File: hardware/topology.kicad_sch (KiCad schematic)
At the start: 0 parts

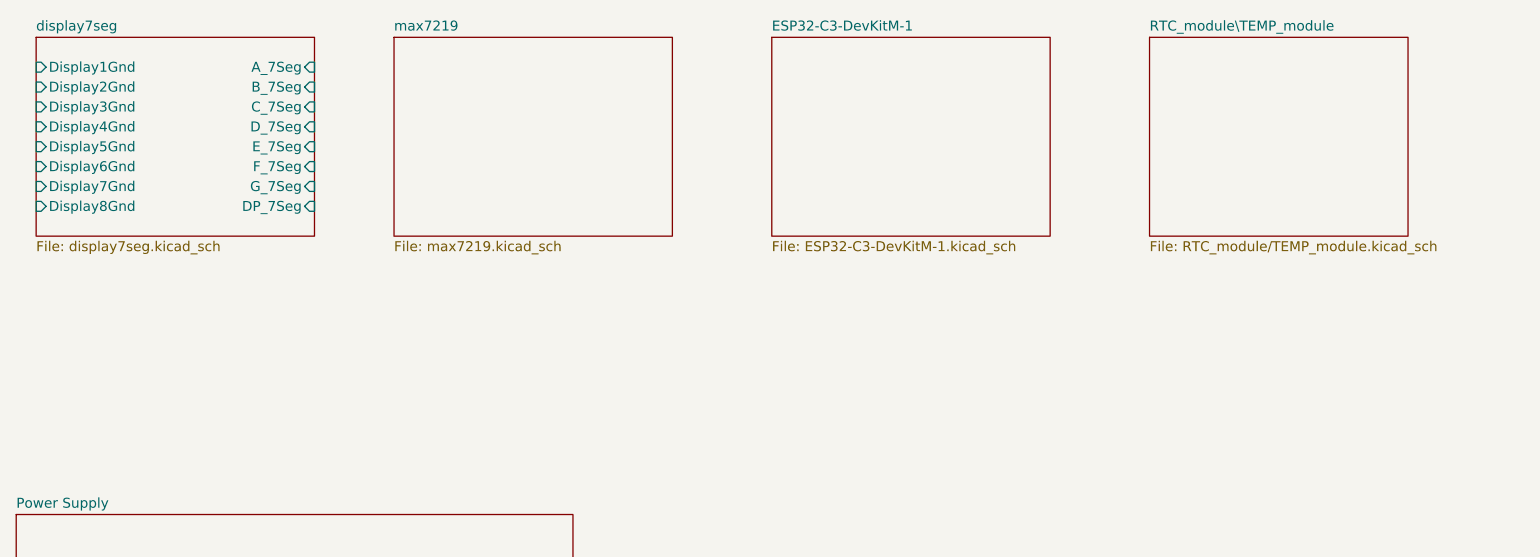
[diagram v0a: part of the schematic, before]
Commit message: Hardware: Rename Temp to RTC-Sensor and Update Schematics
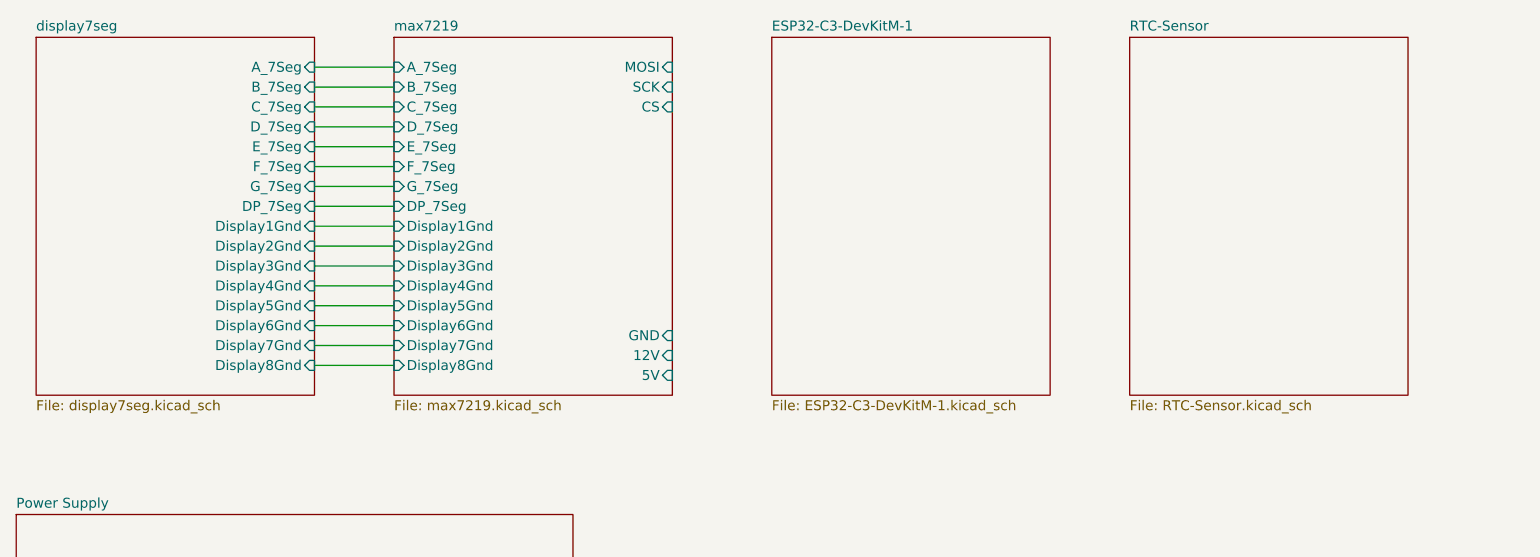
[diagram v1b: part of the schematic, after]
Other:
- removed sheet RTC_module\TEMP_module
- added sheet RTC-Sensor (RTC-Sensor.kicad_sch)
- sheet max7219 ports: added 12V, 5V, A_7Seg, B_7Seg, CS, C_7Seg, DP_7Seg, D_7Seg, Display1Gnd, Display2Gnd, Display3Gnd, Display4Gnd, Display5Gnd, Display6Gnd, Display7Gnd, Display8Gnd, E_7Seg, F_7Seg, GND, G_7Seg, MOSI, SCK; removed none

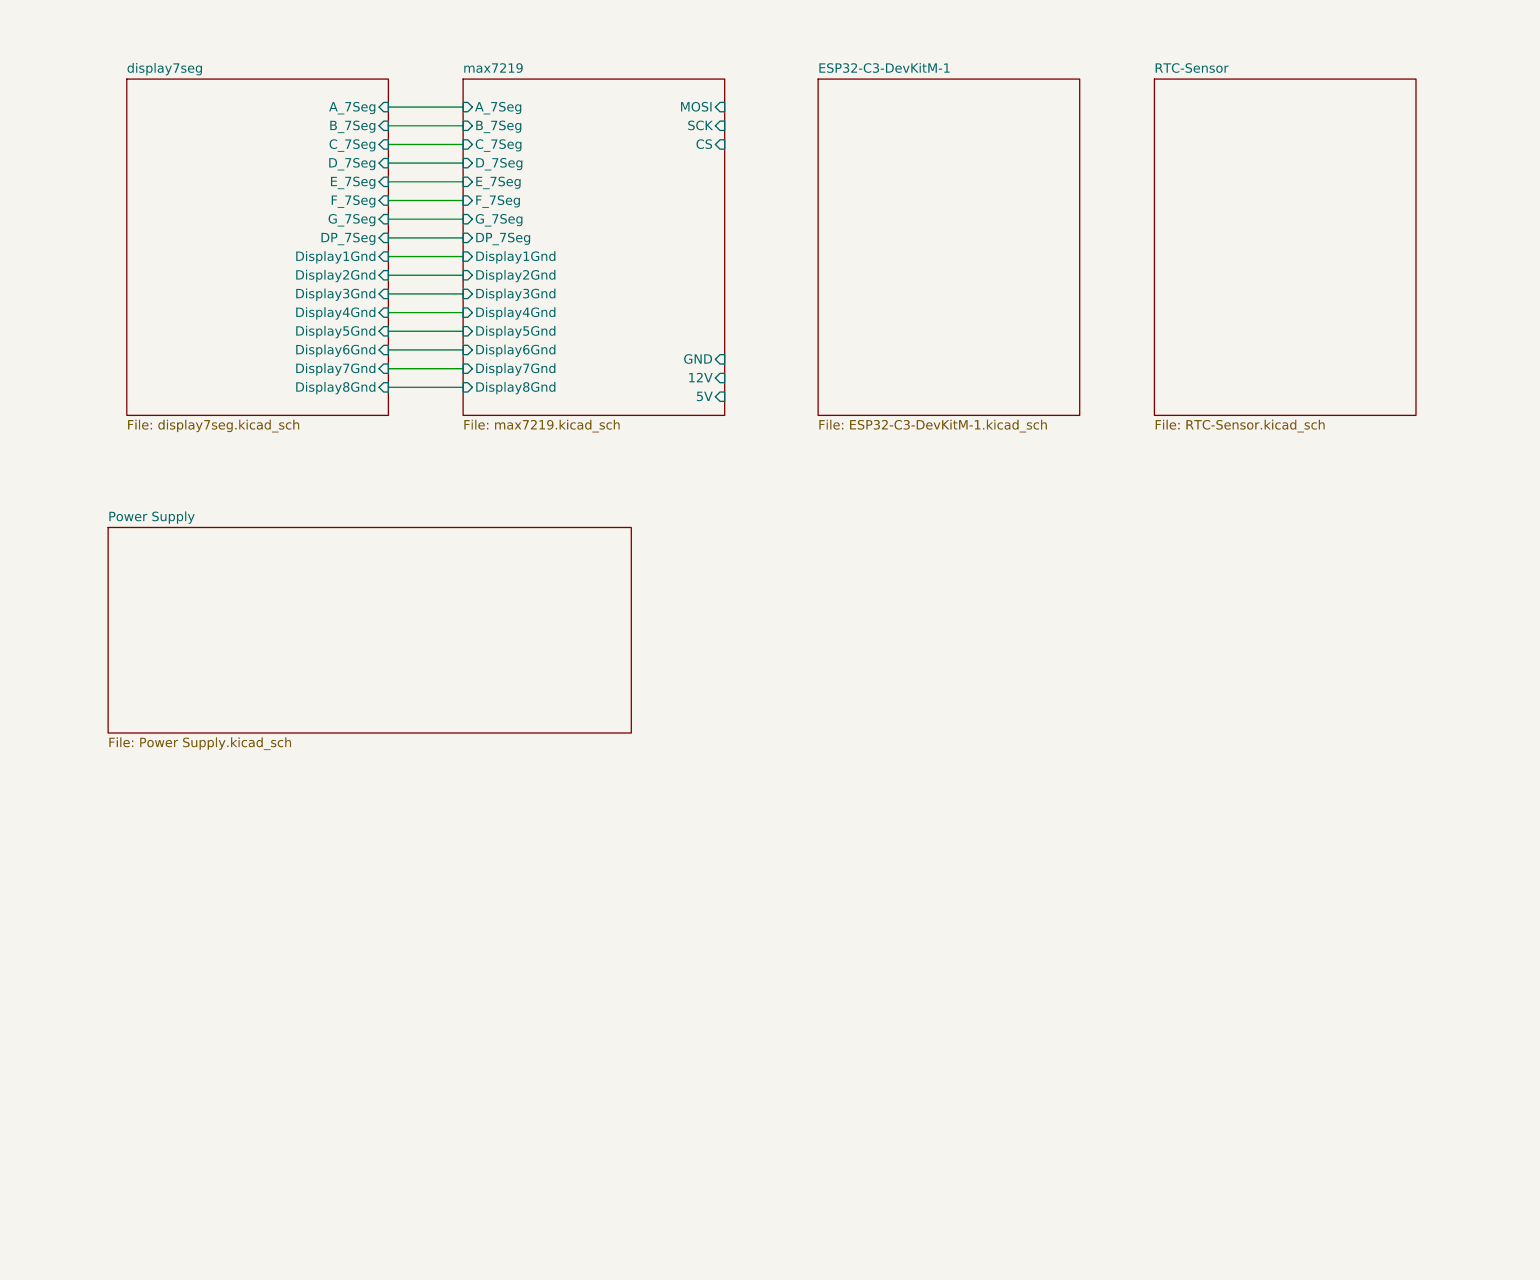
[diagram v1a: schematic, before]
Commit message: Hardware: Updated Schematics and inicial ESP32 schematic
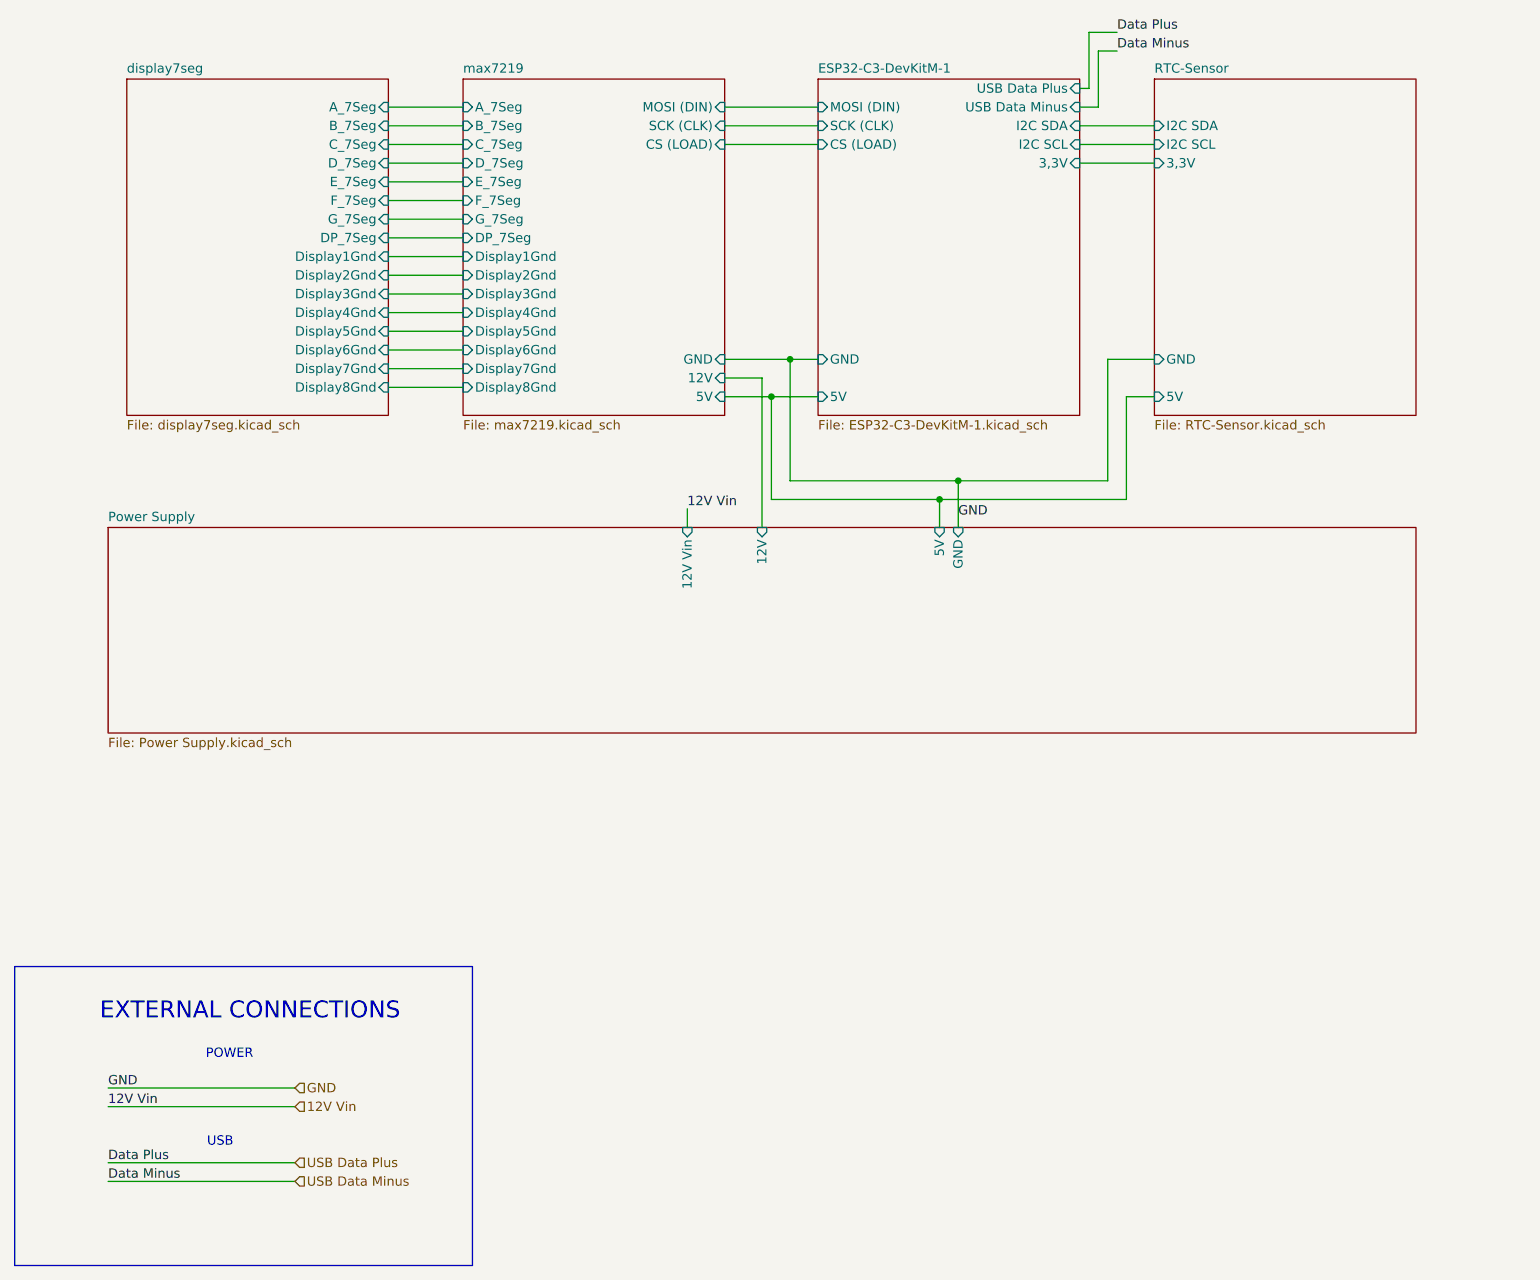
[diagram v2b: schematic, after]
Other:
- sheet ESP32-C3-DevKitM-1 ports: added 3,3V, 5V, CS (LOAD), GND, I2C SCL, I2C SDA, MOSI (DIN), SCK (CLK), USB Data Minus, USB Data Plus; removed none
- sheet Power Supply ports: added 12V, 12V Vin, 5V, GND; removed none
- sheet RTC-Sensor ports: added 3,3V, 5V, GND, I2C SCL, I2C SDA; removed none
- sheet max7219 ports: added CS (LOAD), MOSI (DIN), SCK (CLK); removed CS, MOSI, SCK
- note added: "EXTERNAL CONNECTIONS"
- note added: "POWER"
- note added: "USB"
